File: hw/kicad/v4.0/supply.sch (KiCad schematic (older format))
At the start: 65 parts, among them P3 CONN_01X02, U13 ACT4088, U2 zldo1117, U27 ACT4088, U28 ACT4088

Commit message: Changed 120uf 1808 to 1210 100uF
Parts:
- C103, C104, C105, C106, C107, C108, C120, C121, C122, C96, C99: LCSC C14663 -> C14663
- C109, C110, C111, C123, C124, C131, C132: LCSC C15850 -> C15850
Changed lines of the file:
@@
 F 9 "" H 0   0   50  0001 C CNN "Description"
 F 10 "" H 0   0   50  0001 C CNN "Manufacturer"
-F 11 " C15850" H 8200 5350 50  0001 C CNN "LCSC"
+F 11 "C15850" H 8200 5350 50  0001 C CNN "LCSC"
 	1    8200 5350
 	1    0    0    -1
@@
 F 9 "" H 0   0   50  0001 C CNN "Description"
 F 10 "" H 0   0   50  0001 C CNN "Manufacturer"
-F 11 " C14663" H 6850 4800 50  0001 C CNN "LCSC"
+F 11 "C14663" H 6850 4800 50  0001 C CNN "LCSC"
 	1    6850 4800
 	0    -1   -1   0
@@
 F 9 "" H 0   0   50  0001 C CNN "Description"
 F 10 "" H 0   0   50  0001 C CNN "Manufacturer"
-F 11 " C15850" H 8450 3550 50  0001 C CNN "LCSC"
+F 11 "C15850" H 8450 3550 50  0001 C CNN "LCSC"
 	1    8450 3550
 	1    0    0    -1
@@
 F 9 "" H 0   0   50  0001 C CNN "Description"
 F 10 "" H 0   0   50  0001 C CNN "Manufacturer"
-F 11 " C14663" H 6850 3000 50  0001 C CNN "LCSC"
+F 11 "C14663" H 6850 3000 50  0001 C CNN "LCSC"
 	1    6850 3000
 	0    -1   -1   0
@@
 F 9 "" H 0   0   50  0001 C CNN "Description"
 F 10 "" H 0   0   50  0001 C CNN "Manufacturer"
-F 11 " C14663" H 1200 5350 50  0001 C CNN "LCSC"
+F 11 "C14663" H 1200 5350 50  0001 C CNN "LCSC"
 	1    1200 5350
 	1    0    0    -1
@@
 F 9 "" H 0   0   50  0001 C CNN "Description"
 F 10 "" H 0   0   50  0001 C CNN "Manufacturer"
-F 11 " C14663" H 7700 5350 50  0001 C CNN "LCSC"
+F 11 "C14663" H 7700 5350 50  0001 C CNN "LCSC"
 	1    7700 5350
 	1    0    0    -1
@@
 F 9 "" H 0   0   50  0001 C CNN "Description"
 F 10 "" H 0   0   50  0001 C CNN "Manufacturer"
-F 11 " C14663" H 7700 3550 50  0001 C CNN "LCSC"
+F 11 "C14663" H 7700 3550 50  0001 C CNN "LCSC"
 	1    7700 3550
 	1    0    0    -1
@@
 F 9 "" H 0   0   50  0001 C CNN "Description"
 F 10 "" H 0   0   50  0001 C CNN "Manufacturer"
-F 11 " C14663" H 5050 3550 50  0001 C CNN "LCSC"
+F 11 "C14663" H 5050 3550 50  0001 C CNN "LCSC"
 	1    5050 3550
 	1    0    0    -1
@@
 F 9 "" H 0   0   50  0001 C CNN "Description"
 F 10 "" H 0   0   50  0001 C CNN "Manufacturer"
-F 11 " C14663" H 5000 5350 50  0001 C CNN "LCSC"
+F 11 "C14663" H 5000 5350 50  0001 C CNN "LCSC"
 	1    5000 5350
 	1    0    0    -1
@@
 F 9 "" H 0   0   50  0001 C CNN "Description"
 F 10 "" H 0   0   50  0001 C CNN "Manufacturer"
-F 11 " C14663" H 2450 5350 50  0001 C CNN "LCSC"
+F 11 "C14663" H 2450 5350 50  0001 C CNN "LCSC"
 	1    2450 5350
 	1    0    0    -1
@@
 F 9 "" H 0   0   50  0001 C CNN "Description"
 F 10 "" H 0   0   50  0001 C CNN "Manufacturer"
-F 11 " C15850" H 8200 3550 50  0001 C CNN "LCSC"
+F 11 "C15850" H 8200 3550 50  0001 C CNN "LCSC"
 	1    8200 3550
 	1    0    0    -1
@@
 F 9 "" H 0   0   50  0001 C CNN "Description"
 F 10 "" H 0   0   50  0001 C CNN "Manufacturer"
-F 11 " C15850" H 8450 2050 50  0001 C CNN "LCSC"
+F 11 "C15850" H 8450 2050 50  0001 C CNN "LCSC"
 	1    8450 2050
 	1    0    0    -1
@@
 F 9 "" H 0   0   50  0001 C CNN "Description"
 F 10 "" H 0   0   50  0001 C CNN "Manufacturer"
-F 11 " C14663" H 6850 1500 50  0001 C CNN "LCSC"
+F 11 "C14663" H 6850 1500 50  0001 C CNN "LCSC"
 	1    6850 1500
 	0    -1   -1   0
@@
 F 9 "" H 0   0   50  0001 C CNN "Description"
 F 10 "" H 0   0   50  0001 C CNN "Manufacturer"
-F 11 " C14663" H 7700 2050 50  0001 C CNN "LCSC"
+F 11 "C14663" H 7700 2050 50  0001 C CNN "LCSC"
 	1    7700 2050
 	1    0    0    -1
@@
 F 9 "" H 0   0   50  0001 C CNN "Description"
 F 10 "" H 0   0   50  0001 C CNN "Manufacturer"
-F 11 " C14663" H 5050 2050 50  0001 C CNN "LCSC"
+F 11 "C14663" H 5050 2050 50  0001 C CNN "LCSC"
 	1    5050 2050
 	1    0    0    -1
@@
 F 9 "" H 0   0   50  0001 C CNN "Description"
 F 10 "" H 0   0   50  0001 C CNN "Manufacturer"
-F 11 " C15850" H 8200 2050 50  0001 C CNN "LCSC"
+F 11 "C15850" H 8200 2050 50  0001 C CNN "LCSC"
 	1    8200 2050
 	1    0    0    -1
@@
 F 9 "" H 0   0   50  0001 C CNN "Description"
 F 10 "" H 0   0   50  0001 C CNN "Manufacturer"
-F 11 " C15850" H 8450 5350 50  0001 C CNN "LCSC"
+F 11 "C15850" H 8450 5350 50  0001 C CNN "LCSC"
 	1    8450 5350
 	1    0    0    -1
@@
 F 9 "" H 0   0   50  0001 C CNN "Description"
 F 10 "" H 0   0   50  0001 C CNN "Manufacturer"
-F 11 " C15850" H 2950 5350 50  0001 C CNN "LCSC"
+F 11 "C15850" H 2950 5350 50  0001 C CNN "LCSC"
 	1    2950 5350
 	1    0    0    -1

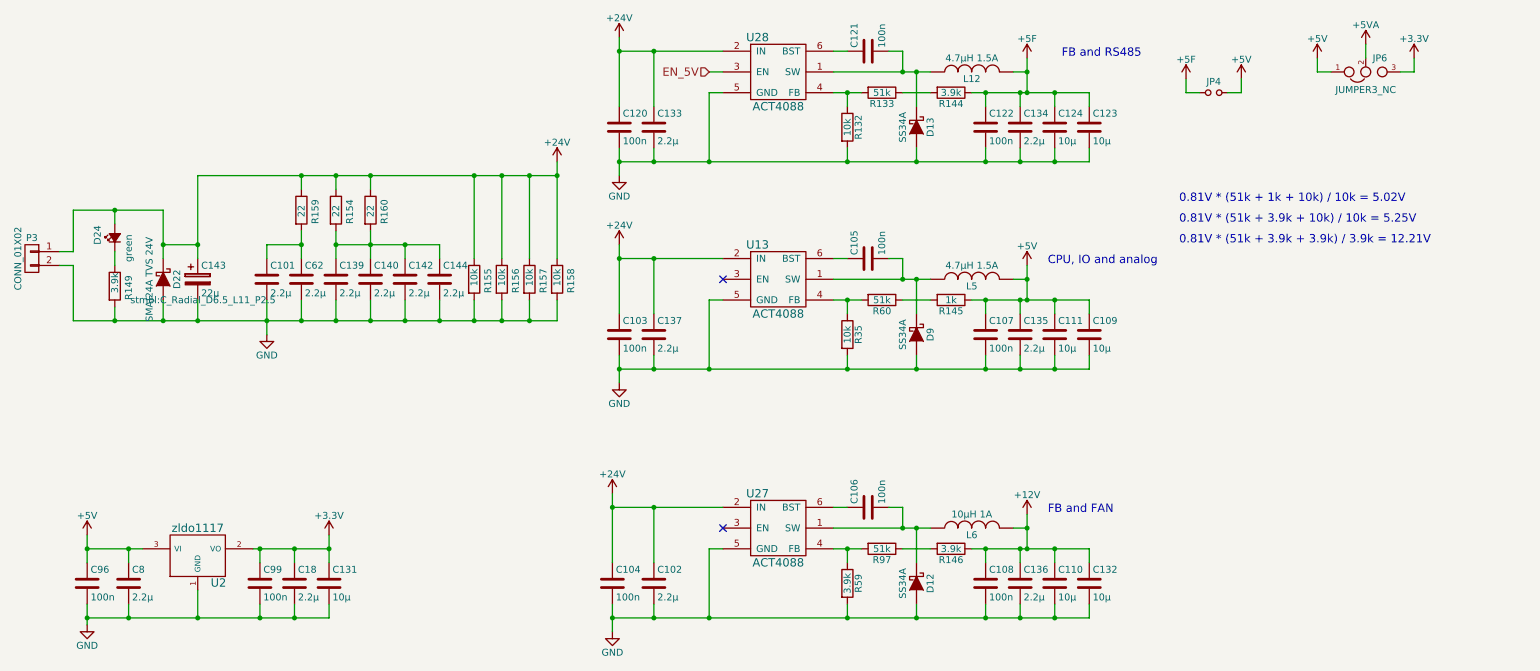
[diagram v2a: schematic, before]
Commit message: Switch some 2.2uf 0603 to 1uf bypass to get 50V version on jlcpcb
Change 2.2uf 0603 to 0805 on iram to get 50V version on jlcpcb
other cleanup
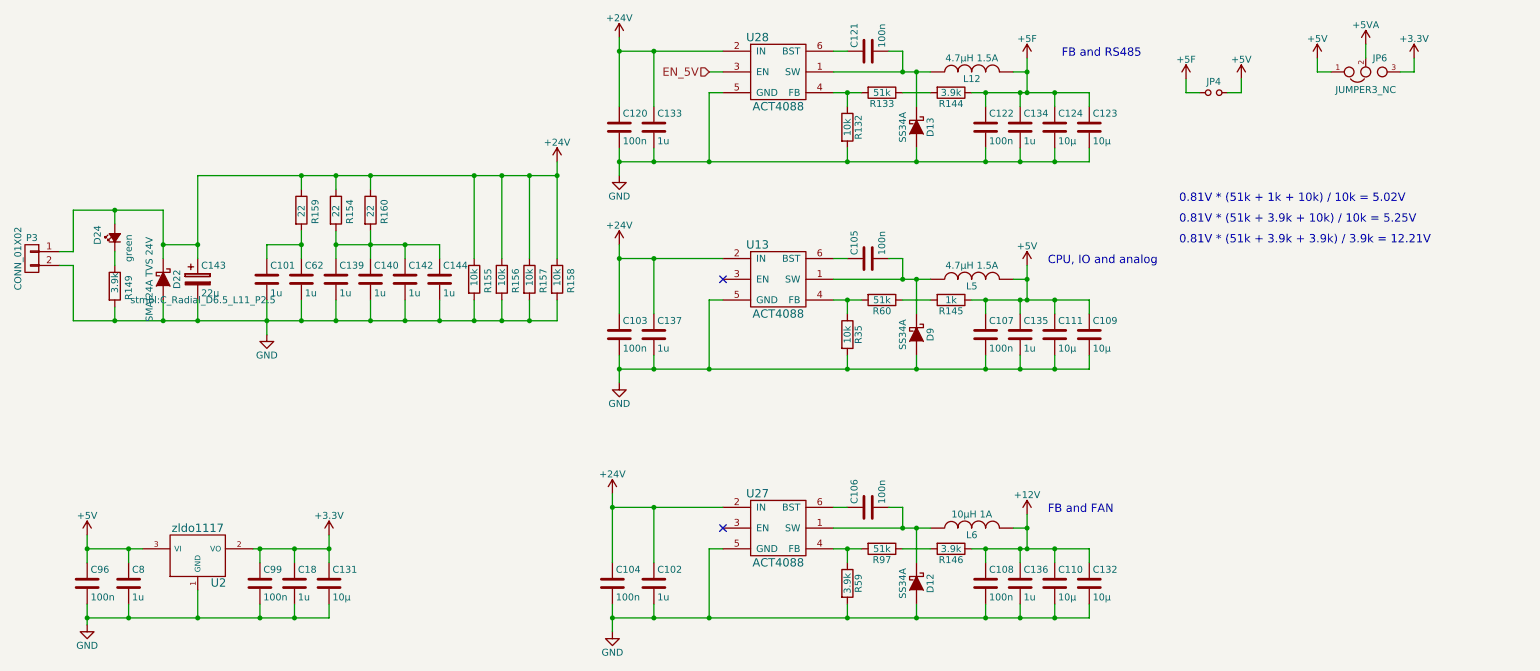
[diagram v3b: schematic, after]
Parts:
- C101, C102, C133, C134, C135, C136, C137, C139, C140, C142, C144, C18, C62, C8: value 2.2µ -> 1u; LCSC C23630 -> C15849; Manufacturer (none) -> Samsung Electro-Mechanics; Manufacturer No (none) -> CL10A105KB8NNNC
- C103, C104, C105, C106, C107, C108, C120, C121, C122, C96, C99: Manufacturer (none) -> YAGEO; Manufacturer No (none) -> CC0603KRX7R9BB104
- C109, C110, C111, C123, C124, C131, C132: Manufacturer (none) -> Samsung Electro-Mechanics; Manufacturer No (none) -> CL21A106KAYNNNE
- C143: LCSC (none) -> C317887; Manufacturer (none) -> Su'scon; Manufacturer No (none) -> SD050M220D11PKKKS00R
- P3: LCSC C441171 -> (none)
